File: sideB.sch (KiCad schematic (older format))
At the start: 40 parts, among them IC1 4520, IC2 LM2902N, IC3 LM555N, J1 USB_2, P1 CONN_2, Q4 NPN, SW4 SW_PUSH

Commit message: First values added.
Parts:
- C2, C4: value C -> 0.1uF
- C3: value C -> 0.01uF
- D13, D14: value DIODE -> 1N4148
- R24: value R -> 10K
- R8, R9: value R -> 4.7K
- RV2: value POT -> 100K
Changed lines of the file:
@@
-EESchema Schematic File Version 2  date Wed 19 Sep 2012 18:42:47 CEST
+EESchema Schematic File Version 2  date Mon 01 Oct 2012 00:30:51 CEST
 LIBS:power
 LIBS:device
@@
 Sheet 1 1
 Title "SMT4dummies - sideB"
-Date "19 sep 2012"
+Date "30 sep 2012"
 Rev "1"
 Comp "d-Squared Robotics"
@@
 P 2150 5300
 F 0 "C2" H 2200 5400 50  0000 L CNN
-F 1 "C" H 2200 5200 50  0000 L CNN
+F 1 "0.1uF" H 2200 5200 50  0000 L CNN
 	1    2150 5300
 	1    0    0    -1
@@
 P 4900 6050
 F 0 "C4" H 4950 6150 50  0000 L CNN
-F 1 "C" H 4950 5950 50  0000 L CNN
+F 1 "0.1uF" H 4950 5950 50  0000 L CNN
 	1    4900 6050
 	1    0    0    -1
@@
 P 4900 5400
 F 0 "R24" V 4980 5400 50  0000 C CNN
-F 1 "R" V 4900 5400 50  0000 C CNN
+F 1 "10K" V 4900 5400 50  0000 C CNN
 	1    4900 5400
 	1    0    0    -1
@@
 P 2550 5300
 F 0 "C3" H 2600 5400 50  0000 L CNN
-F 1 "C" H 2600 5200 50  0000 L CNN
+F 1 "0.01uF" H 2600 5200 50  0000 L CNN
 	1    2550 5300
 	1    0    0    -1
@@
 P 1750 4600
 F 0 "D13" H 1750 4700 40  0000 C CNN
-F 1 "DIODE" H 1750 4500 40  0000 C CNN
+F 1 "1N4148" H 1750 4500 40  0000 C CNN
 	1    1750 4600
 	0    -1   -1   0
@@
 P 2550 4600
 F 0 "D14" H 2550 4700 40  0000 C CNN
-F 1 "DIODE" H 2550 4500 40  0000 C CNN
+F 1 "1N4148" H 2550 4500 40  0000 C CNN
 	1    2550 4600
 	0    1    1    0
@@
 P 2150 4400
 F 0 "RV2" H 2150 4300 50  0000 C CNN
-F 1 "POT" H 2150 4400 50  0000 C CNN
+F 1 "100K" H 2150 4400 50  0000 C CNN
 	1    2150 4400
 	1    0    0    -1
@@
 P 2550 2000
 F 0 "R8" V 2630 2000 50  0000 C CNN
-F 1 "R" V 2550 2000 50  0000 C CNN
+F 1 "4.7K" V 2550 2000 50  0000 C CNN
 	1    2550 2000
 	-1   0    0    1
@@
 P 3750 2600
 F 0 "R9" V 3830 2600 50  0000 C CNN
-F 1 "R" V 3750 2600 50  0000 C CNN
+F 1 "4.7K" V 3750 2600 50  0000 C CNN
 	1    3750 2600
 	1    0    0    -1

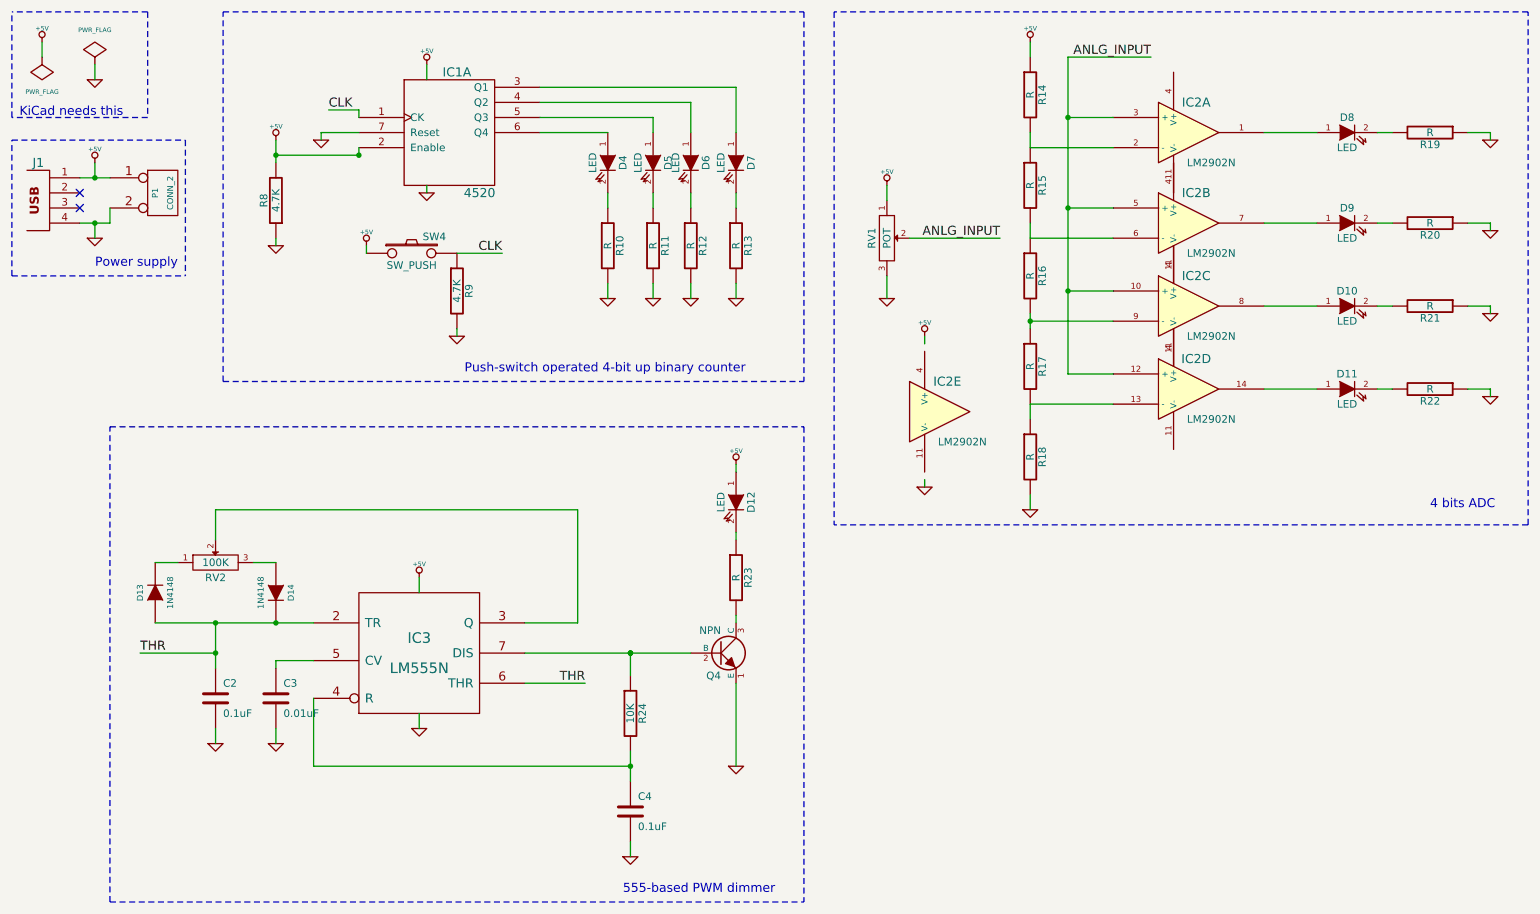
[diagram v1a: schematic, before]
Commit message: 555 circuit changed.
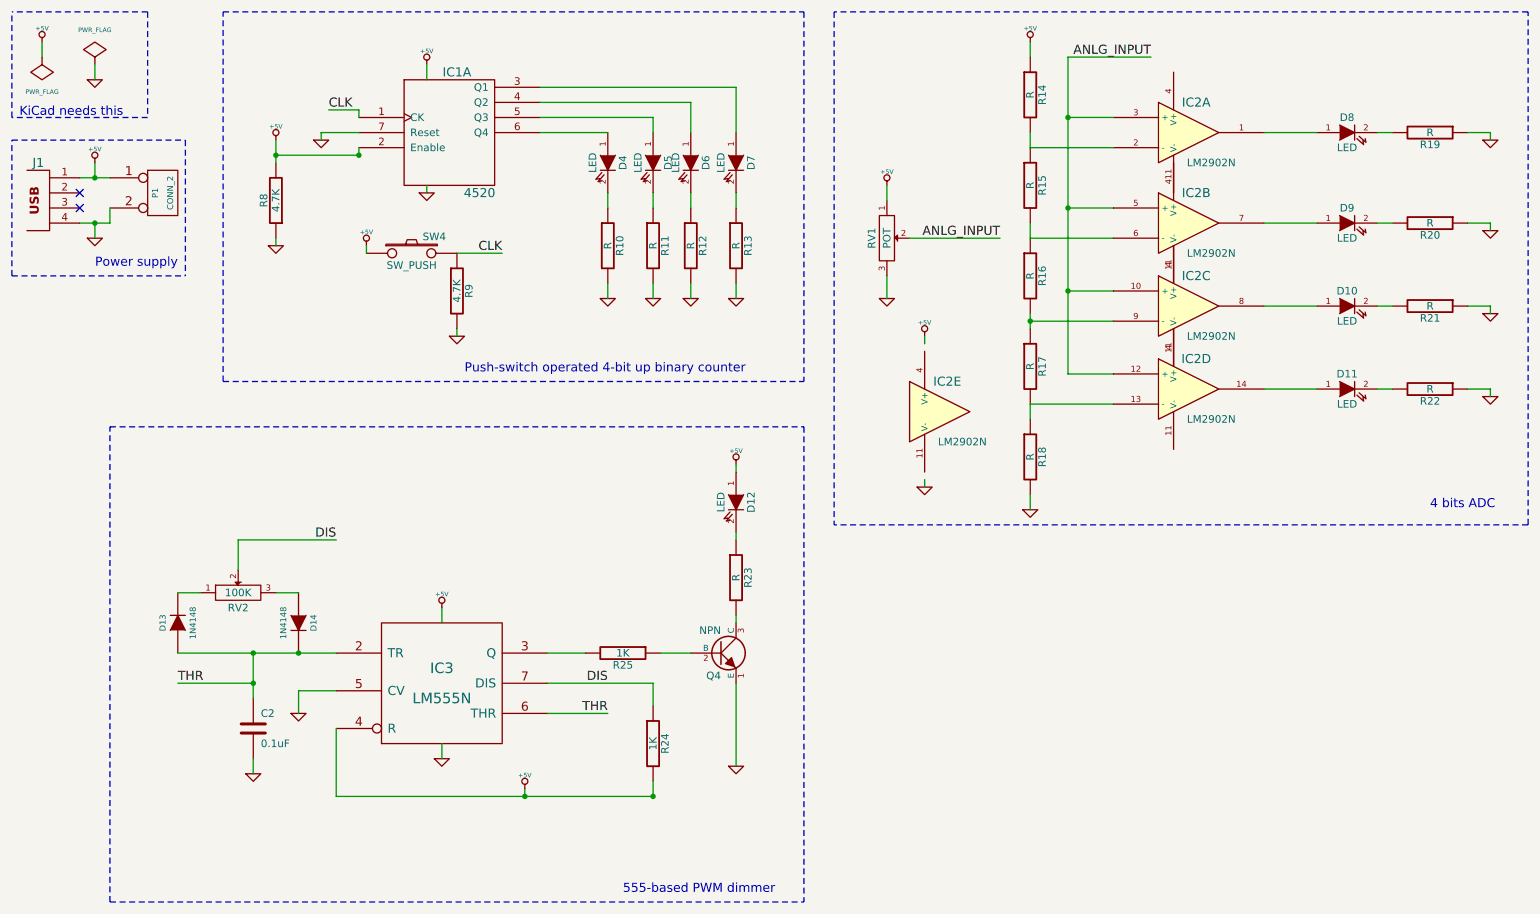
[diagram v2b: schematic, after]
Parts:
- removed C3: 0.01uF, symbol C
- removed C4: 0.1uF, symbol C
- added R25: 1K, symbol R
- R24: value 10K -> 1K
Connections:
- net +5V: now also IC3.4 (R), R24.2
- net GND: now also IC3.5 (CV)
- net at IC3.3 (Q): now also R25.2; no longer RV2.2
- net DIS: now reaches IC3.7 (DIS), R24.1
- net DIS: now also RV2.2; no longer Q4.2 (B)
- new net: Q4.2 (B), R25.1
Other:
- moved on the sheet: C2, D13, D14, IC3, R24, RV2
